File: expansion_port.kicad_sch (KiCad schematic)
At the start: 1 part, among them J3 Conn_02x30_Odd_Even

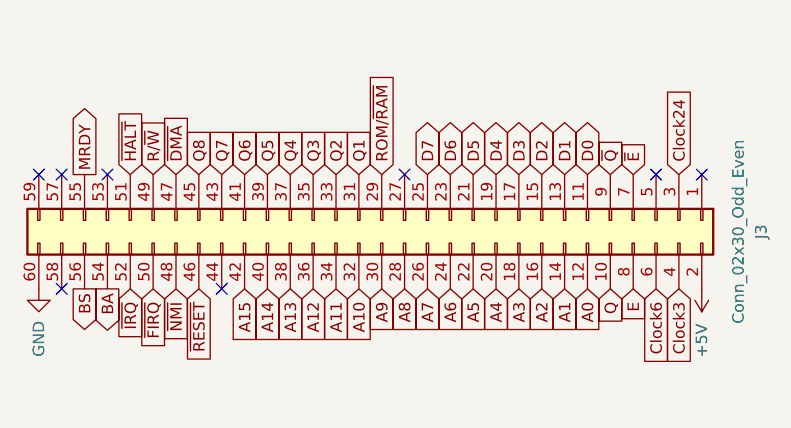
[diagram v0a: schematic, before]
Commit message: add mapped memory lane
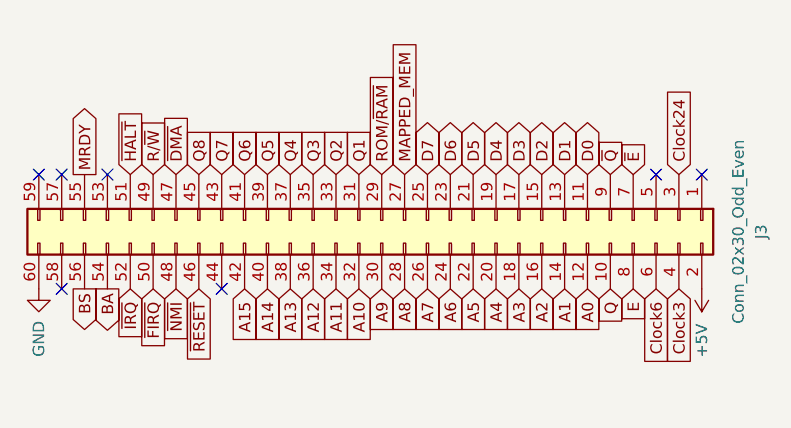
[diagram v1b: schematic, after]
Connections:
- net MAPPED_MEM: now reaches J3.27 (Pin_27)
- no-connect marks 8 -> 7
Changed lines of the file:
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@@
   (paper "A4")
   (no_connect (at 102.362 58.039))
-  (no_connect (at 143.002 58.039))
   (no_connect (at 104.902 70.739))
   (no_connect (at 122.682 70.739))
@@
     )
   )
+  (global_label "MAPPED_MEM" (shape input) (at 143.002 58.039 90) (fields_autoplaced)
+    (effects (font (size 1.27 1.27)) (justify left))
+    (property "Intersheet References" "${INTERSHEET_REFS}" (id 0) (at 142.9226 43.1073 90)
+      (effects (font (size 1.27 1.27)) (justify left) hide)
+    )
+  )
